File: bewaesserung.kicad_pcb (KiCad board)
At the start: 2 copper layers, 100 x 70 mm, 28 parts, among them J1 vom Raspberry Pi, J2 Ventil GPIO 2, J3 Ventil GPIO 3, J4 Ventil GPIO 15, J5 Netzanschluss 230V AC, K1 PE014005, K2 PE014005, K3 PE014005, K4 PE014005, Q1 IRLML0100, Q2 IRLML0100, Q3 IRLML0100, Q4 IRLML0100, T1 VC10_1_24

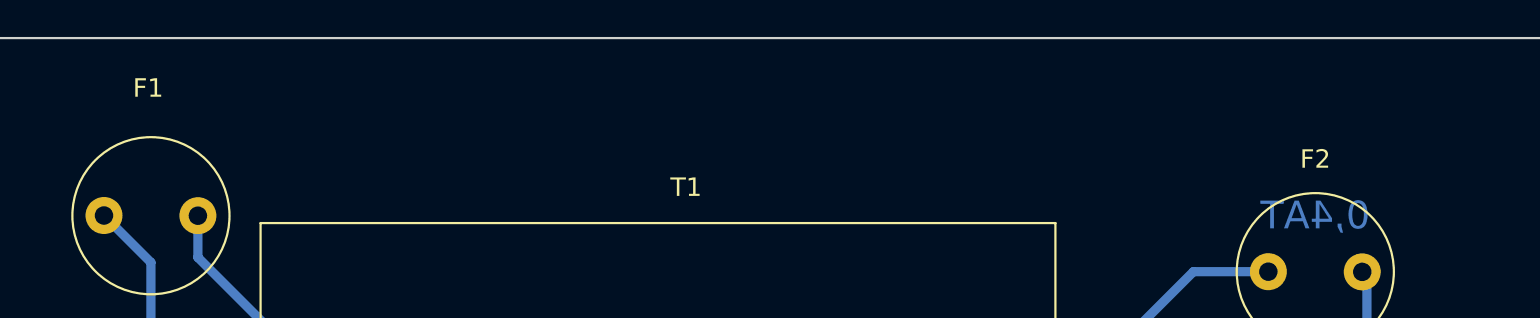
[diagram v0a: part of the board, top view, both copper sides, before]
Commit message: Sicherungen angepasst
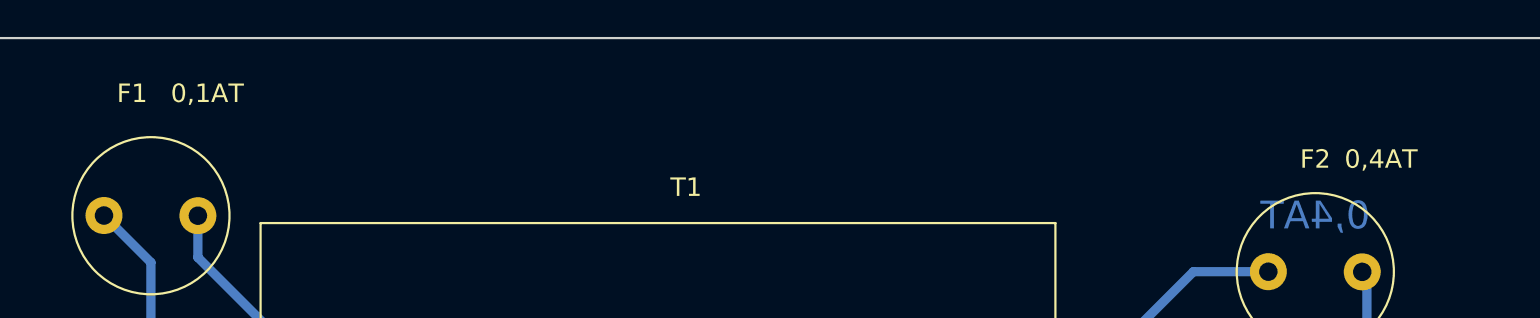
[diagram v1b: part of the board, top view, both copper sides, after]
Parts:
- added ?: , , F.Cu at (-59.9, -34.0)
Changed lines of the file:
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@@
-(kicad_pcb (version 20171130) (host pcbnew 5.1.4+dfsg1-1)
+(kicad_pcb (version 20171130) (host pcbnew 5.1.5+dfsg1-2build2)
   (general
     (thickness 1.6)
@@
     (tracks 181)
     (zones 0)
-    (modules 28)
+    (modules 29)
     (nets 32)
   )
@@
     (add_net GND)
   )
+  (module "" (layer F.Cu)
+    (at -59.944 -34.036)
+    (fp_text reference "" (at -34.036 -1.016) (layer F.SilkS)
+      (effects (font (size 1.27 1.27) (thickness 0.15)))
+    )
+    (fp_text value "" (at -34.036 -1.016) (layer F.SilkS)
+      (effects (font (size 1.27 1.27) (thickness 0.15)))
+    )
+    (fp_text user 0,1AT (at 28.956 2.032 -180) (layer F.SilkS)
+      (effects (font (size 1 1) (thickness 0.15)))
+    )
+  )
   (module Gerold:Schraubklemme_4-fach (layer F.Cu)
     (at -34.036 -1.016 90)
@@
       (effects (font (size 1 1) (thickness 0.15)))
     )
-    (fp_text value 0,4AT (at 2.39 7.43) (layer F.Fab)
+    (fp_text value 0,4AT (at -1.016 6.096) (layer F.SilkS)
       (effects (font (size 1 1) (thickness 0.15)))
     )
@@
     (descr "Fuse, Fuseholder, TR5, Littelfuse/Wickmann, No. 460, No560, https://www.littelfuse.com/~/media/electronics/datasheets/fuse_holders/littelfuse_fuse_holder_559_560_datasheet.pdf.pdf")
     (tags "Fuse Fuseholder TR5 Littelfuse/Wickmann No. 460 No560 ")
-    (fp_text reference F1 (at 2.39 -6.89) (layer F.SilkS)
-      (effects (font (size 1 1) (thickness 0.15)))
-    )
+    (fp_text reference F1 (at 1.524 -6.604) (layer F.SilkS)
+      (effects (font (size 1 1) (thickness 0.15)))
+    )
